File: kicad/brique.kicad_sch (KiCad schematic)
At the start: 51 parts, among them J1 Conn_01x07, J2 USB_B_Micro, J3 Speaker Pads, J4 Battery Connection Pads, J6 BM03B-SRSS-TB, J7 BM03B-SRSS-TB, M1 Vibration, Q1 BC847, SW2 BOOT, U1 W25Q128JVS, U5 RP2350_80QFN, Y1 ABM8-272-T3, Y2 RV-3028-C7_32.768kHz_1ppm_TA_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

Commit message: replace standard pcba part with economic
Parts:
- C11, C12, C13, C14, C15, C16, C17, C18, C2, C20, C21, C25, C5, C79, C8: JLCPCB C77020 -> C1525
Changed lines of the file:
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@@
 			)
 		)
-		(property "JLCPCB" "C77020"
+		(property "JLCPCB" "C1525"
 			(at 240.03 43.18 0)
 			(effects
@@
 			)
 		)
-		(property "JLCPCB" "C77020"
+		(property "JLCPCB" "C1525"
 			(at 297.18 43.18 0)
 			(effects
@@
 			)
 		)
-		(property "JLCPCB" "C77020"
+		(property "JLCPCB" "C1525"
 			(at 262.89 43.18 0)
 			(effects
@@
 			)
 		)
-		(property "JLCPCB" "C77020"
+		(property "JLCPCB" "C1525"
 			(at 382.27 217.17 0)
 			(effects
@@
 			)
 		)
-		(property "JLCPCB" "C77020"
+		(property "JLCPCB" "C1525"
 			(at 308.61 43.18 0)
 			(effects
@@
 			)
 		)
-		(property "JLCPCB" "C77020"
+		(property "JLCPCB" "C1525"
 			(at 68.58 113.03 0)
 			(effects
@@
 			)
 		)
-		(property "JLCPCB" "C77020"
+		(property "JLCPCB" "C1525"
 			(at 285.75 43.18 0)
 			(effects
@@
 			)
 		)
-		(property "JLCPCB" "C77020"
+		(property "JLCPCB" "C1525"
 			(at 322.58 143.51 0)
 			(effects
@@
 			)
 		)
-		(property "JLCPCB" "C77020"
+		(property "JLCPCB" "C1525"
 			(at 274.32 43.18 0)
 			(effects
@@
 			)
 		)
-		(property "JLCPCB" "C77020"
+		(property "JLCPCB" "C1525"
 			(at 355.6 229.87 0)
 			(effects
@@
 			)
 		)
-		(property "JLCPCB" "C77020"
+		(property "JLCPCB" "C1525"
 			(at 320.04 43.18 0)
 			(effects
@@
 			)
 		)
-		(property "JLCPCB" "C77020"
+		(property "JLCPCB" "C1525"
 			(at 187.96 68.58 0)
 			(effects
@@
 			)
 		)
-		(property "JLCPCB" "C77020"
+		(property "JLCPCB" "C1525"
 			(at 251.46 43.18 0)
 			(effects
@@
 			)
 		)
-		(property "JLCPCB" "C77020"
+		(property "JLCPCB" "C1525"
 			(at 161.29 68.58 0)
 			(effects
@@
 			)
 		)
-		(property "JLCPCB" "C77020"
+		(property "JLCPCB" "C1525"
 			(at 331.47 43.18 0)
 			(effects

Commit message: update c25 to prevent bom aggregation
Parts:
- C25: footprint Capacitor_SMD:C_0402_1005Metric -> Capacitor_SMD:C_0805_2012Metric; JLCPCB C1525 -> C49678
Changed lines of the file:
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@@
 			)
 		)
-		(property "Footprint" "Capacitor_SMD:C_0402_1005Metric"
+		(property "Footprint" "Capacitor_SMD:C_0805_2012Metric"
 			(at 386.08 216.2048 0)
 			(effects
@@
 			)
 		)
-		(property "JLCPCB" "C1525"
+		(property "JLCPCB" "C49678"
 			(at 382.27 217.17 0)
 			(effects

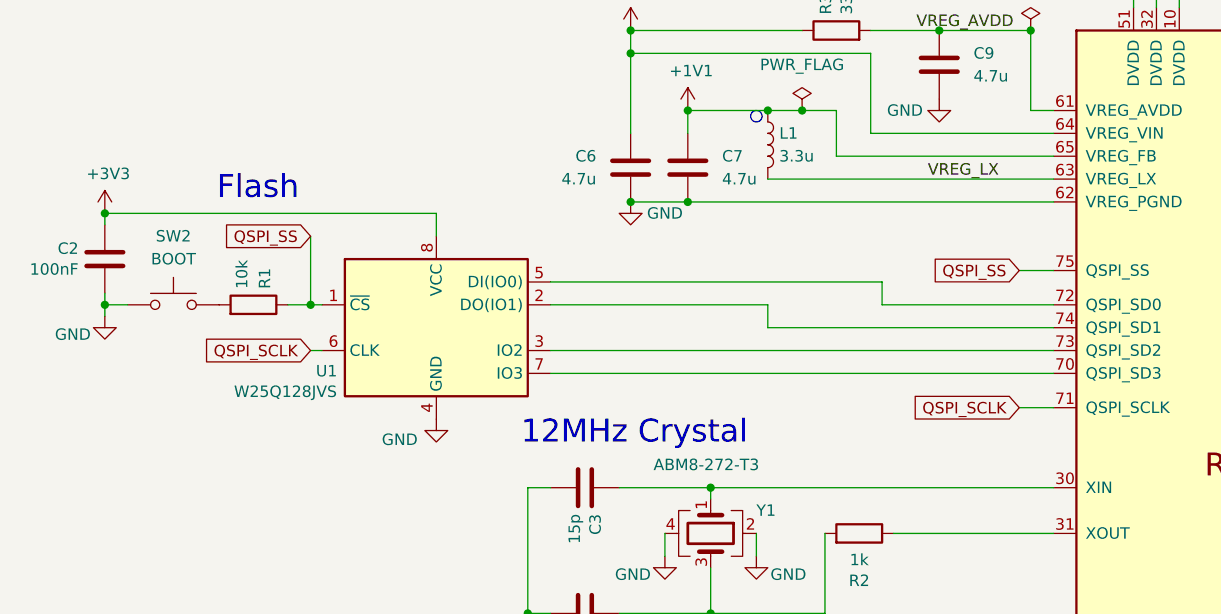
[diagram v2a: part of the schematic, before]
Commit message: remove flash
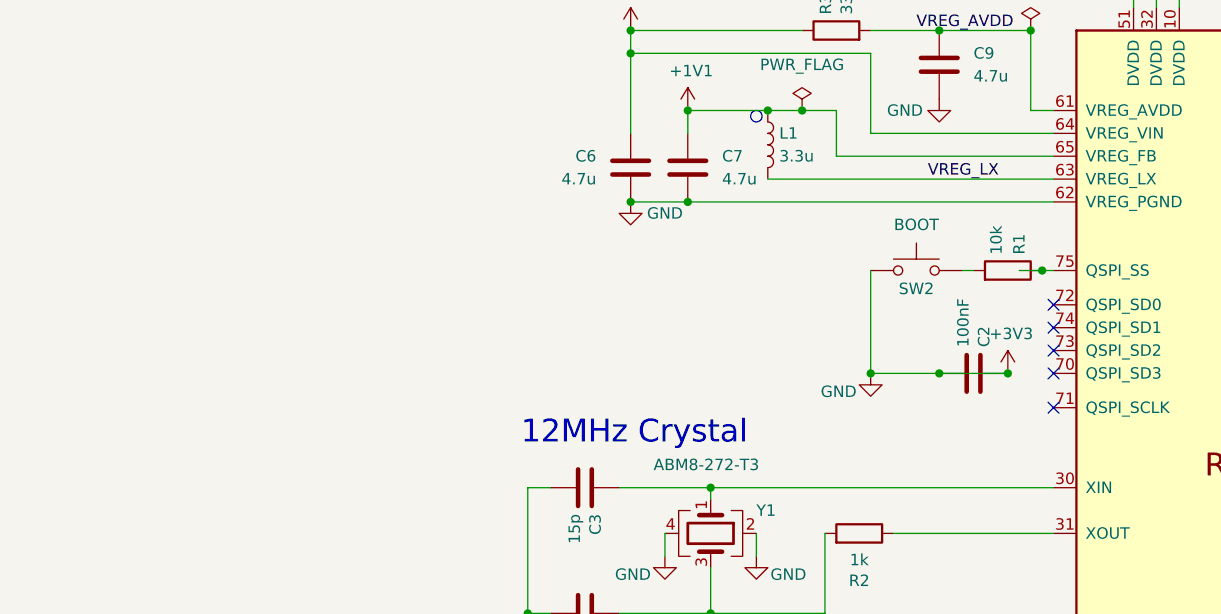
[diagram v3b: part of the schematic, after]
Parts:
- removed U1: W25Q128JVS, Package_SO:SOIC-8_5.23x5.23mm_P1.27mm, symbol Memory_Flash:W25Q128JVS
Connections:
- net GND is gone; now on net +3V3: C10.1, C11.1, C12.2, C13.2, C14.2, C15.2, C16.2, C17.2, C18.2, C19.2, C2.2, C20.2, C21.2, C25.2, C3.2, C4.2, C5.2, C6.2, C7.2, C79.1, C8.1, C9.2, J1.6 (Pin_6), J2.5 (GND), J2.6 (Shield), J3.2 (Pin_2), J4.4 (Pin_4), J6.2 (Pin_2), J6.MP (MountPin), J7.2 (Pin_2), J7.MP (MountPin), LS1.2, Q1.2 (E), R41.1, SW2.1, U5.10 (DVDD), U5.32 (DVDD), U5.51 (DVDD), U5.62 (VREG_PGND), U5.81 (GND), Y1.2, Y1.4, Y2.5 (VSS)
- net QSPI_SCLK: no longer names the net of U5.71 (QSPI_SCLK)
- net QSPI_SS: no longer names the net of R1.1, U5.75 (QSPI_SS)
- no-connect marks 19 -> 24
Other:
- note removed: "Flash"
- moved on the sheet: C2, R1, SW2

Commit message: remove pull ups
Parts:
- removed C2: 100nF, Capacitor_SMD:C_0402_1005Metric, symbol Device:C
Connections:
- net +3V3: no longer C10.1, C11.1, C12.2, C13.2, C14.2, C15.2, C16.2, C17.2, C18.2, C19.2, C20.2, C21.2, C25.2, C3.2, C4.2, C5.2, C6.2, C7.2, C79.1, C8.1, C9.2, J1.6 (Pin_6), J2.5 (GND), J2.6 (Shield), J3.2 (Pin_2), J4.4 (Pin_4), J6.2 (Pin_2), J6.MP (MountPin), J7.2 (Pin_2), J7.MP (MountPin), LS1.2, Q1.2 (E), R41.1, SW2.1, U5.10 (DVDD), U5.32 (DVDD), U5.51 (DVDD), U5.62 (VREG_PGND), U5.81 (GND), Y1.2, Y1.4, Y2.5 (VSS)
- new net GND: C10.1, C11.1, C12.2, C13.2, C14.2, C15.2, C16.2, C17.2, C18.2, C19.2, C20.2, C21.2, C25.2, C3.2, C4.2, C5.2, C6.2, C7.2, C79.1, C8.1, C9.2, J1.6 (Pin_6), J2.5 (GND), J2.6 (Shield), J3.2 (Pin_2), J4.4 (Pin_4), J6.2 (Pin_2), J6.MP (MountPin), J7.2 (Pin_2), J7.MP (MountPin), LS1.2, Q1.2 (E), R41.1, SW2.1, U5.10 (DVDD), U5.32 (DVDD), U5.51 (DVDD), U5.62 (VREG_PGND), U5.81 (GND), Y1.2, Y1.4, Y2.5 (VSS)
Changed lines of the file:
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@@
 	)
 	(junction
-		(at 153.67 125.73)
-		(diameter 0)
-		(color 0 0 0 0)
-	)
-	(junction
 		(at 127 87.63)
 		(diameter 0)
@@
 	)
 	(junction
-		(at 168.91 125.73)
-		(diameter 0)
-		(color 0 0 0 0)
-	)
-	(junction
 		(at 161.29 72.39)
 		(diameter 0)
@@
 	)
 	(junction
-		(at 161.29 125.73)
-		(diameter 0)
-		(color 0 0 0 0)
-	)
-	(junction
 		(at 217.17 72.39)
 		(diameter 0)
@@
 	(wire
 		(pts
-			(xy 161.29 125.73) (xy 168.91 125.73)
-		)
-		(stroke
-			(width 0)
-			(type default)
-		)
-	)
-	(wire
-		(pts
 			(xy 205.74 232.41) (xy 205.74 234.95)
 		)
@@
 	(wire
 		(pts
-			(xy 161.29 125.73) (xy 153.67 125.73)
-		)
-		(stroke
-			(width 0)
-			(type default)
-		)
-	)
-	(wire
-		(pts
 			(xy 187.96 72.39) (xy 185.42 72.39)
 		)
@@
 	(wire
 		(pts
-			(xy 153.67 114.3) (xy 153.67 125.73)
+			(xy 153.67 114.3) (xy 153.67 118.11)
 		)
 		(stroke
@@
 	)
 	(symbol
-		(lib_id "power:+3V3")
-		(at 168.91 125.73 0)
-		(unit 1)
-		(exclude_from_sim no)
-		(in_bom yes)
-		(on_board yes)
-		(dnp no)
-		(property "Reference" "#PWR026"
-			(at 168.91 129.54 0)
-			(effects
-				(font
-					(size 1.27 1.27)
-				)
-				(hide yes)
-			)
-		)
-		(property "Value" "+3V3"
-			(at 169.291 121.3358 0)
-			(effects
-				(font
-					(size 1.27 1.27)
-				)
-			)
-		)
-		(property "Footprint" ""
-			(at 168.91 125.73 0)
-			(effects
-				(font
-					(size 1.27 1.27)
-				)
-				(hide yes)
-			)
-		)
-		(property "Datasheet" ""
-			(at 168.91 125.73 0)
-			(effects
-				(font
-					(size 1.27 1.27)
-				)
-				(hide yes)
-			)
-		)
-		(property "Description" ""
-			(at 168.91 125.73 0)
-			(effects
-				(font
-					(size 1.27 1.27)
-				)
-				(hide yes)
-			)
-		)
-		(pin "1"
-		)
-		(instances
-			(project "brique"
-				(path "/3906e17f-1a23-46f4-8c63-f34176cde9d9"
-					(reference "#PWR026")
-					(unit 1)
-				)
-			)
-		)
-	)
-	(symbol
 		(lib_id "Connector_Generic_MountingPin:Conn_01x03_MountingPin")
 		(at 262.89 97.79 270)
@@
 	)
 	(symbol
-		(lib_id "Device:C")
-		(at 165.1 125.73 270)
-		(mirror x)
-		(unit 1)
-		(exclude_from_sim no)
-		(in_bom yes)
-		(on_board yes)
-		(dnp no)
-		(property "Reference" "C2"
-			(at 166.2684 122.809 0)
-			(effects
-				(font
-					(size 1.27 1.27)
-				)
-				(justify left)
-			)
-		)
-		(property "Value" "100nF"
-			(at 163.957 122.809 0)
-			(effects
-				(font
-					(size 1.27 1.27)
-				)
-				(justify left)
-			)
-		)
-		(property "Footprint" "Capacitor_SMD:C_0402_1005Metric"
-			(at 161.29 124.7648 0)
-			(effects
-				(font
-					(size 1.27 1.27)
-				)
-				(hide yes)
-			)
-		)
-		(property "Datasheet" "~"
-			(at 165.1 125.73 0)
-			(effects
-				(font
-					(size 1.27 1.27)
-				)
-				(hide yes)
-			)
-		)
-		(property "Description" ""
-			(at 165.1 125.73 0)
-			(effects
-				(font
-					(size 1.27 1.27)
-				)
-				(hide yes)
-			)
-		)
-		(property "JLCPCB" "C1525"
-			(at 165.1 125.73 0)
-			(effects
-				(font
-					(size 1.27 1.27)
-				)
-				(hide yes)
-			)
-		)
-		(pin "1"
-		)
-		(pin "2"
-		)
-		(instances
-			(project "brique"
-				(path "/3906e17f-1a23-46f4-8c63-f34176cde9d9"
-					(reference "C2")
-					(unit 1)
-				)
-			)
-		)
-	)
-	(symbol
 		(lib_id "power:GND")
 		(at 161.29 95.25 0)
@@
 	(symbol
 		(lib_id "power:GND")
-		(at 153.67 125.73 0)
+		(at 153.67 118.11 0)
 		(unit 1)
 		(exclude_from_sim no)
@@
 		(dnp no)
 		(property "Reference" "#PWR048"
-			(at 153.67 132.08 0)
+			(at 153.67 124.46 0)
 			(effects
 				(font
@@
 		)
 		(property "Value" "GND"
-			(at 150.114 127.762 0)
+			(at 150.114 120.142 0)
 			(effects
 				(font
@@
 		)
 		(property "Footprint" ""
-			(at 153.67 125.73 0)
+			(at 153.67 118.11 0)
 			(effects
 				(font
@@
 		)
 		(property "Datasheet" ""
-			(at 153.67 125.73 0)
+			(at 153.67 118.11 0)
 			(effects
 				(font
@@
 		)
 		(property "Description" ""
-			(at 153.67 125.73 0)
+			(at 153.67 118.11 0)
 			(effects
 				(font

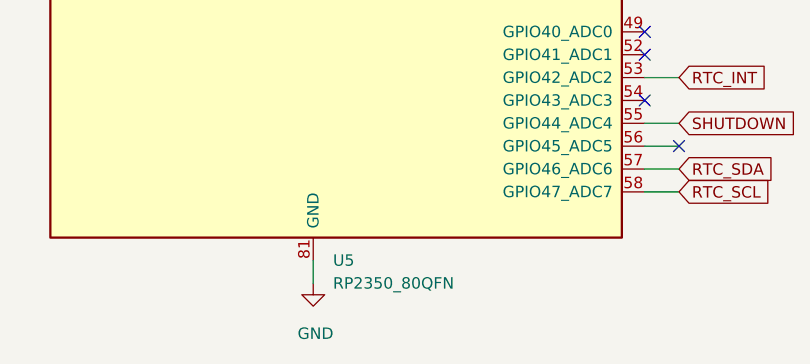
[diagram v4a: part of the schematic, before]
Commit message: update some references for new unavailable chip
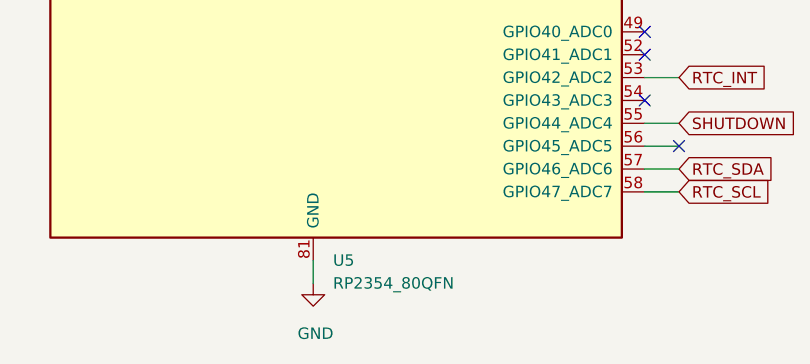
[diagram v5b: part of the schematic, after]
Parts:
- U5: value RP2350_80QFN -> RP2354_80QFN; JLCPCB C42415655 -> (none)
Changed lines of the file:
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@@
 			)
 		)
-		(property "Value" "RP2350_80QFN"
+		(property "Value" "RP2354_80QFN"
 			(at 207.9341 234.95 0)
 			(effects
@@
 			)
 		)
-		(property "JLCPCB" "C42415655"
+		(property "JLCPCB" ""
 			(at 205.74 135.89 0)
 			(effects

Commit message: fill in JLCPCB part number
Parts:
- U5: JLCPCB (none) -> C39843328
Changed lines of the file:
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@@
 			)
 		)
-		(property "JLCPCB" ""
+		(property "JLCPCB" "C39843328"
 			(at 205.74 135.89 0)
 			(effects
